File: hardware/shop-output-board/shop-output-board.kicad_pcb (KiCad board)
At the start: 2 copper layers, 150 x 115 mm, 84 parts

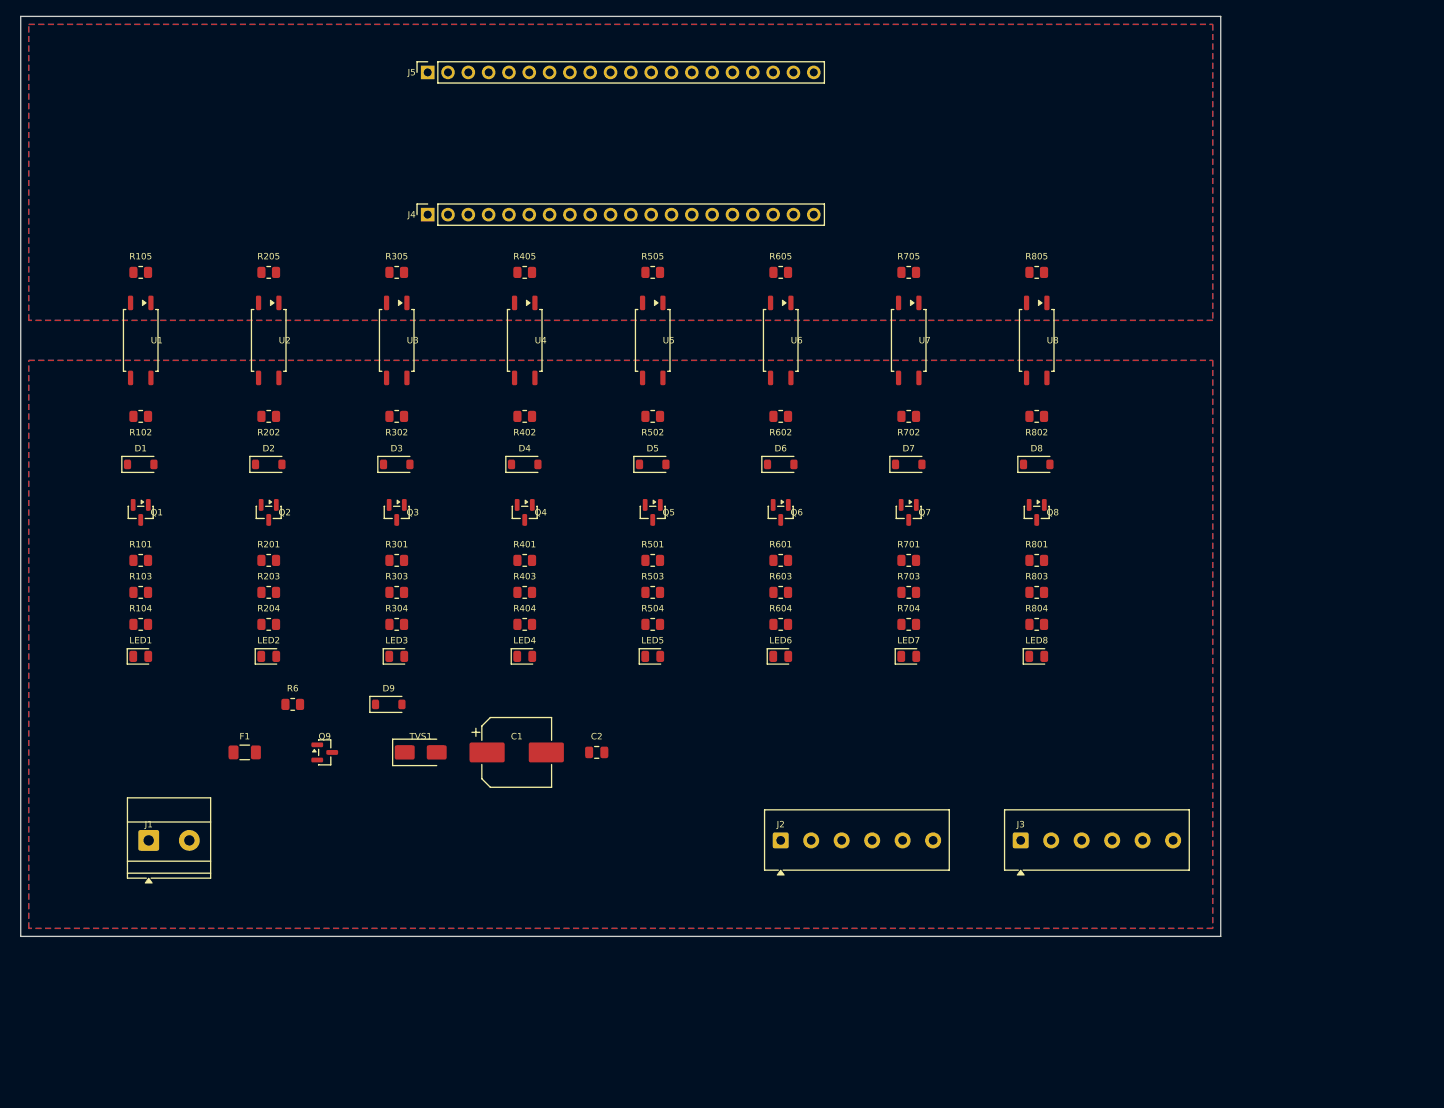
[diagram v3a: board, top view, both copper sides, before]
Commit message: stop the generator overwriting a board that has been routed
The board file stopped being a generated artefact the moment it was opened in
Pcbnew and routed - it now holds 260 segments this script cannot reproduce.
Re-running generate_pcb.py would have discarded all of it without a word.

It now refuses if the target already contains segments, and says what to do
instead. --force is there for a deliberate restart.

Co-Authored-By: Claude Opus 5 <noreply@anthropic.com>
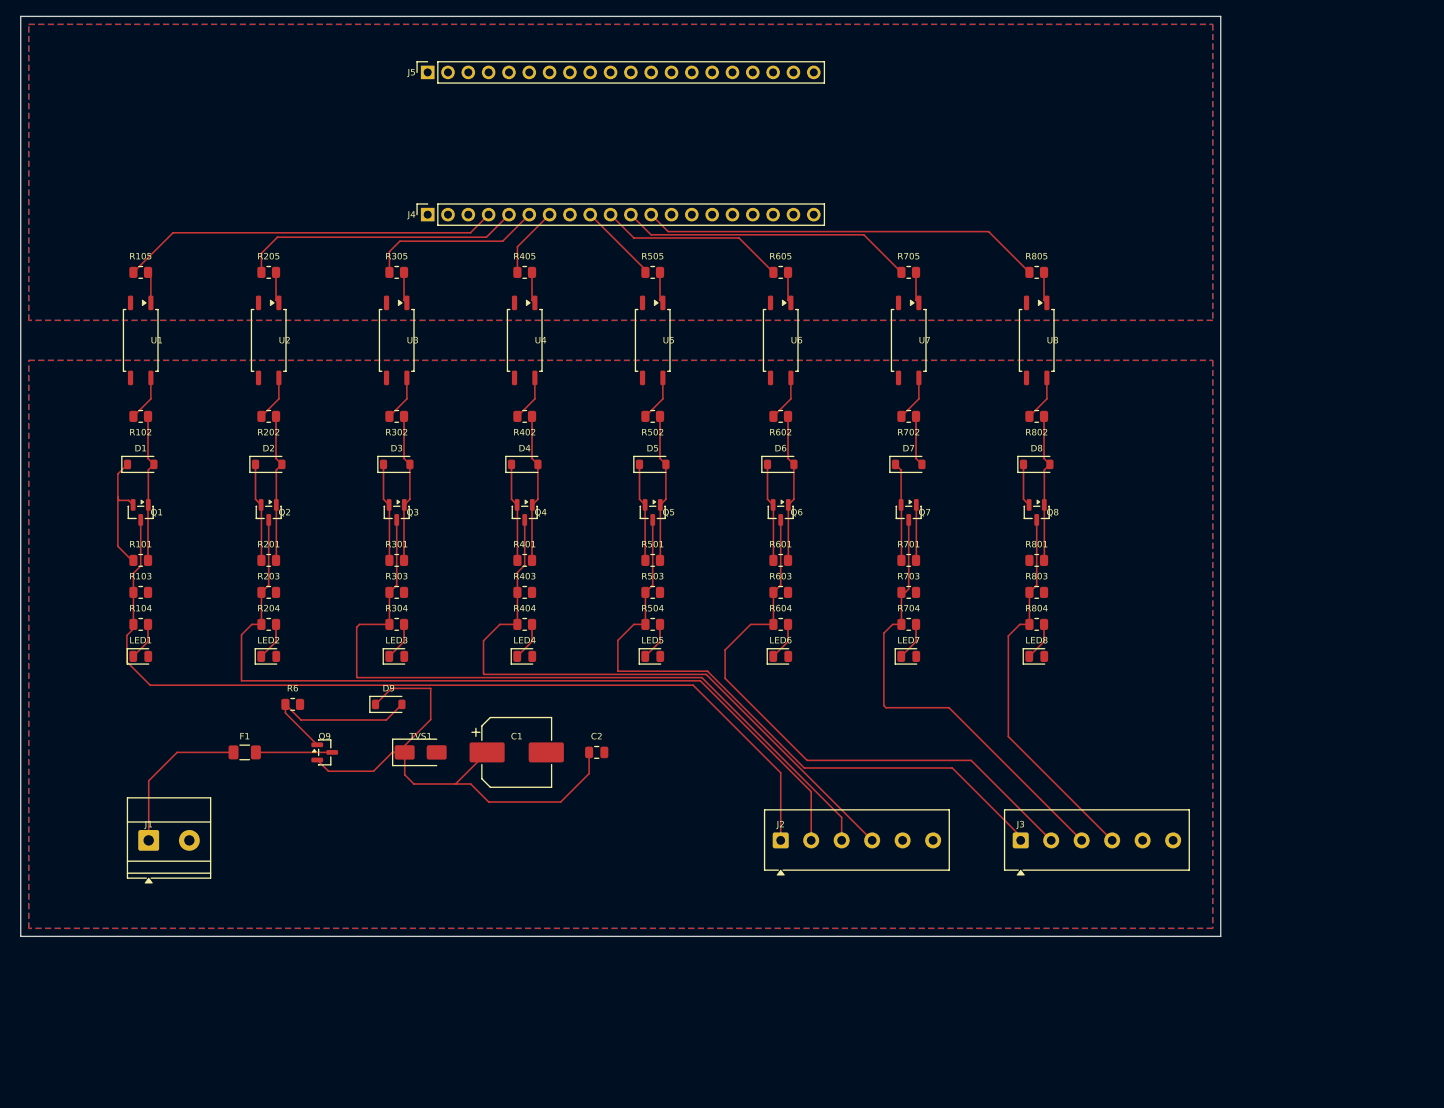
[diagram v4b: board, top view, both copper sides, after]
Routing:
- net V+: track 0.00 -> 161.6 mm
- net OUT1: track 0.00 -> 114.5 mm
- net OUT2: track 0.00 -> 105.3 mm
- net OUT3: track 0.00 -> 94.7 mm
- net OUT5: track 0.00 -> 81.0 mm
- net OUT4: track 0.00 -> 79.9 mm
- net OUT6: track 0.00 -> 73.5 mm
- net OUT7: track 0.00 -> 57.1 mm
- net GP9: track 0.00 -> 50.3 mm
- net OUT8: track 0.00 -> 47.6 mm
- net GP2: track 0.00 -> 47.4 mm
- net GP8: track 0.00 -> 36.8 mm
- net GP3: track 0.00 -> 35.3 mm
- net GP7: track 0.00 -> 23.3 mm
- net Q9GATE: track 0.00 -> 22.9 mm
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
